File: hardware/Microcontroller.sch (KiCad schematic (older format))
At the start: 18 parts, among them J4 ICSP, J5 SERIAL_OUT, Q1 2N3904, U4 ATMEGA64M1

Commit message: Modified schematic to use one less op-amp and a cheaper microcontroller
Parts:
- removed U4: ATMEGA64M1, TQFP-32, symbol ATMEGA64M1
- added C12, C13: 18pF, 0805, symbol C
- added U3: ATMEGA328-A, TQFP32, symbol ATMEGA328-A
- added X1: 20MHz, HC49, symbol CRYSTAL
- renumbered C11 to C10, C14 to C11, C15 to C14, C12 to C8, C13 to C9, R14 to R10, R15 to R11, R16 to R12, R17 to R13, R18 to R14, R19 to R15, R13 to R9
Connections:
- net labels added: CURR_SENSE, MISO, MOSI, SCK
- net labels removed: U_CURR_SENSE, V_CURR_SENSE, W_CURR_SENSE
- wire segments 63 -> 73
- no-connect marks 10 -> 5
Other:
- moved on the sheet: C10, C11, C8, C9, R12

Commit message: Modified schemdatic to use a single PWM channel, similar to Atmel's app note.
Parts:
- added C21: 1uF, 0805, symbol C
- added D4: LED, symbol LED
- added R14: 11k, 0805, symbol R
- added R19: 1k, 0805, symbol R
- added SW1: SW_PUSH, symbol SW_PUSH
- added U4: 74LV08, symbol 74LS08
- C11, C14: value 1000pF -> 2000pF
- R10: renamed from R9; value 10.2K -> 11K
- R11: renamed from R10; value 10.2K -> 11K
- R12: renamed from R11; value 10.2K -> 11K
- R13: renamed from R12; value 10.2K -> 11k
- R16: renamed from R14; value 57.6K -> 169k
- R17: renamed from R15; value 10.2K -> 11k
- renumbered JP1 to J5, J5 to J6, R13 to R15
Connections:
- net labels added: DEBUG_LED, PWM, U_HI_EN, V_HI_EN, W_HI_EN
- net labels removed: BATT_PWM
- wire segments 73 -> 98
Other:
- moved on the sheet: C14, J4, J5, J6, Q1, R10, R11, R12, R15, R16, R17

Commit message: Changed most parts to be through hole to simplify the initial prototype assembly
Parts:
- removed C21: 1uF, 0805, symbol C
- removed L1: 1k @ 100MHz, 0805, symbol INDUCTOR
- removed U3: ATMEGA328-A, TQFP32, symbol ATMEGA328-A
- added C15: 2000pF, symbol C
- added U3: ATMEGA328-P, DIL28, symbol ATMEGA328-P
- C10, C8, C9: footprint 0805 -> (none); Digikey P/N 1276-3010-1-ND -> 445-8517-ND; Mfg P/N CL21F105ZBFNNNE -> FK24X7R1H105K; Mouser P/N (none) -> 810-FK24X7R1H105K
- C11: footprint 0805 -> (none); Digikey P/N 1276-1020-1-ND -> 1268PH-ND; Mfg P/N CL21B102KBANNNC -> S202M29Z5UN63L6R; Mouser P/N (none) -> 594-S202M29Z5UN63L6R
- C12, C13: footprint 0805 -> (none); Digikey P/N 1276-1107-1-ND -> 445-4762-ND; Mfg P/N CL21C180JBANNNC -> FK18C0G1H180J; Mouser P/N (none) -> 810-FK18C0G1H180J
- C14: value 2000pF -> 1uF; footprint 0805 -> (none); Digikey P/N 1276-1020-1-ND -> 445-8517-ND; Mfg P/N CL21B102KBANNNC -> FK24X7R1H105K; Mouser P/N (none) -> 810-FK24X7R1H105K
- R10, R11, R12: value 11K -> 11k; footprint 0805 -> (none); Digikey P/N P10.2KCCT-ND -> 11.0KXBK-ND; Mfg P/N ERJ-6ENF1022V -> MFR-25FBF52-11K; Mouser P/N 667-ERJ-6ENF1022V -> 603-MFR-25FBF52-11K
- R13, R14, R17: footprint 0805 -> (none); Digikey P/N P10.2KCCT-ND -> 11.0KXBK-ND; Mfg P/N ERJ-6ENF1022V -> MFR-25FBF52-11K; Mouser P/N 667-ERJ-6ENF1022V -> 603-MFR-25FBF52-11K
- R15: value 1K -> 1k; footprint 0805 -> (none); Digikey P/N P1.00KCCT-ND -> 1.00KXBK-ND; Mfg P/N ERJ-6ENF1001V -> MFR-25FBF52-1K; Mouser P/N 667-ERJ-6ENF1001V -> 603-MFR-25FBF52-1K
- R16: footprint 0805 -> (none); Digikey P/N P56.2KCCT-ND -> 169KXBK-ND; Mfg P/N ERJ-6ENF5622V -> MFR-25FBF52-169K; Mouser P/N 667-ERJ-6ENF5622V -> 603-MFR-25FBF52-169K
- R19: footprint 0805 -> (none); Digikey P/N P10.2KCCT-ND -> 1.00KXBK-ND; Mfg P/N ERJ-6ENF1022V -> MFR-25FBF52-1K; Mouser P/N 667-ERJ-6ENF1022V -> 603-MFR-25FBF52-1K
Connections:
- net labels removed: +5VA
- wire segments 98 -> 93
- no-connect marks 5 -> 3

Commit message: Added inital layout revision.
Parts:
- U4: value 74LV08 -> 74HC08; Digikey P/N 296-26531-1-ND -> 296-1570-5-ND; Mfg P/N SN74LV08ADR -> SN74HC08N; Mouser P/N 595-SN74LV08ADR -> 595-SN74HC08N
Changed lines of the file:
@@
-EESchema Schematic File Version 2  date Wed 20 May 2015 21:52:57 MST
+EESchema Schematic File Version 2  date Sun 14 Jun 2015 10:56:58 MST
 LIBS:power
 LIBS:device
@@
 Sheet 3 4
 Title "Microcontroller and Support"
-Date "21 may 2015"
+Date "14 jun 2015"
 Rev ""
 Comp ""
@@
 Comment4 ""
 $EndDescr
+$Comp
+L 74LS08 U4
+U 4 1 557DAFC6
+P 8350 3800
+F 0 "U4" H 8350 3850 60  0000 C CNN
+F 1 "74HC08" H 8350 3750 60  0000 C CNN
+F 3 "datasheets/sn74hc08.pdf" H 8350 3800 60  0001 C CNN
+F 4 "SN74HC08N" H 8350 3800 60  0001 C CNN "Mfg P/N"
+F 5 "296-1570-5-ND" H 8350 3800 60  0001 C CNN "Digikey P/N"
+F 6 "595-SN74HC08N" H 8350 3800 60  0001 C CNN "Mouser P/N"
+	4    8350 3800
+	1    0    0    -1
+$EndComp
+$Comp
+L 74LS08 U4
+U 3 1 557DAFC4
+P 8350 3350
+F 0 "U4" H 8350 3400 60  0000 C CNN
+F 1 "74HC08" H 8350 3300 60  0000 C CNN
+F 3 "datasheets/sn74hc08.pdf" H 8350 3350 60  0001 C CNN
+F 4 "SN74HC08N" H 8350 3350 60  0001 C CNN "Mfg P/N"
+F 5 "296-1570-5-ND" H 8350 3350 60  0001 C CNN "Digikey P/N"
+F 6 "595-SN74HC08N" H 8350 3350 60  0001 C CNN "Mouser P/N"
+	3    8350 3350
+	1    0    0    -1
+$EndComp
+$Comp
+L 74LS08 U4
+U 2 1 557DAFC2
+P 8350 2900
+F 0 "U4" H 8350 2950 60  0000 C CNN
+F 1 "74HC08" H 8350 2850 60  0000 C CNN
+F 3 "datasheets/sn74hc08.pdf" H 8350 2900 60  0001 C CNN
+F 4 "SN74HC08N" H 8350 2900 60  0001 C CNN "Mfg P/N"
+F 5 "296-1570-5-ND" H 8350 2900 60  0001 C CNN "Digikey P/N"
+F 6 "595-SN74HC08N" H 8350 2900 60  0001 C CNN "Mouser P/N"
+	2    8350 2900
+	1    0    0    -1
+$EndComp
 $Comp
 L ATMEGA328-P U3
@@
 $Comp
 L 74LS08 U4
-U 4 1 554593C7
-P 8350 3800
-F 0 "U4" H 8350 3850 60  0000 C CNN
-F 1 "74LV08" H 8350 3750 60  0000 C CNN
-F 3 "datasheets/sn74lv08a.pdf" H 8350 3800 60  0001 C CNN
-F 4 "SN74LV08ADR" H 8350 3800 60  0001 C CNN "Mfg P/N"
-F 5 "296-26531-1-ND" H 8350 3800 60  0001 C CNN "Digikey P/N"
-F 6 "595-SN74LV08ADR" H 8350 3800 60  0001 C CNN "Mouser P/N"
-	4    8350 3800
-	1    0    0    -1
-$EndComp
-$Comp
-L 74LS08 U4
-U 3 1 554593C5
-P 8350 3350
-F 0 "U4" H 8350 3400 60  0000 C CNN
-F 1 "74LV08" H 8350 3300 60  0000 C CNN
-F 3 "datasheets/sn74lv08a.pdf" H 8350 3350 60  0001 C CNN
-F 4 "SN74LV08ADR" H 8350 3350 60  0001 C CNN "Mfg P/N"
-F 5 "296-26531-1-ND" H 8350 3350 60  0001 C CNN "Digikey P/N"
-F 6 "595-SN74LV08ADR" H 8350 3350 60  0001 C CNN "Mouser P/N"
-	3    8350 3350
-	1    0    0    -1
-$EndComp
-$Comp
-L 74LS08 U4
-U 2 1 554593C3
-P 8350 2900
-F 0 "U4" H 8350 2950 60  0000 C CNN
-F 1 "74LV08" H 8350 2850 60  0000 C CNN
-F 3 "datasheets/sn74lv08a.pdf" H 8350 2900 60  0001 C CNN
-F 4 "SN74LV08ADR" H 8350 2900 60  0001 C CNN "Mfg P/N"
-F 5 "296-26531-1-ND" H 8350 2900 60  0001 C CNN "Digikey P/N"
-F 6 "595-SN74LV08ADR" H 8350 2900 60  0001 C CNN "Mouser P/N"
-	2    8350 2900
-	1    0    0    -1
-$EndComp
-$Comp
-L 74LS08 U4
 U 1 1 554592E1
 P 8350 2250
 F 0 "U4" H 8350 2300 60  0000 C CNN
-F 1 "74LV08" H 8350 2200 60  0000 C CNN
-F 3 "datasheets/sn74lv08a.pdf" H 8350 2250 60  0001 C CNN
-F 4 "SN74LV08ADR" H 8350 2250 60  0001 C CNN "Mfg P/N"
-F 5 "296-26531-1-ND" H 8350 2250 60  0001 C CNN "Digikey P/N"
-F 6 "595-SN74LV08ADR" H 8350 2250 60  0001 C CNN "Mouser P/N"
+F 1 "74HC08" H 8350 2200 60  0000 C CNN
+F 3 "datasheets/sn74hc08.pdf" H 8350 2250 60  0001 C CNN
+F 4 "SN74HC08N" H 8350 2250 60  0001 C CNN "Mfg P/N"
+F 5 "296-1570-5-ND" H 8350 2250 60  0001 C CNN "Digikey P/N"
+F 6 "595-SN74HC08N" H 8350 2250 60  0001 C CNN "Mouser P/N"
 	1    8350 2250
 	1    0    0    -1

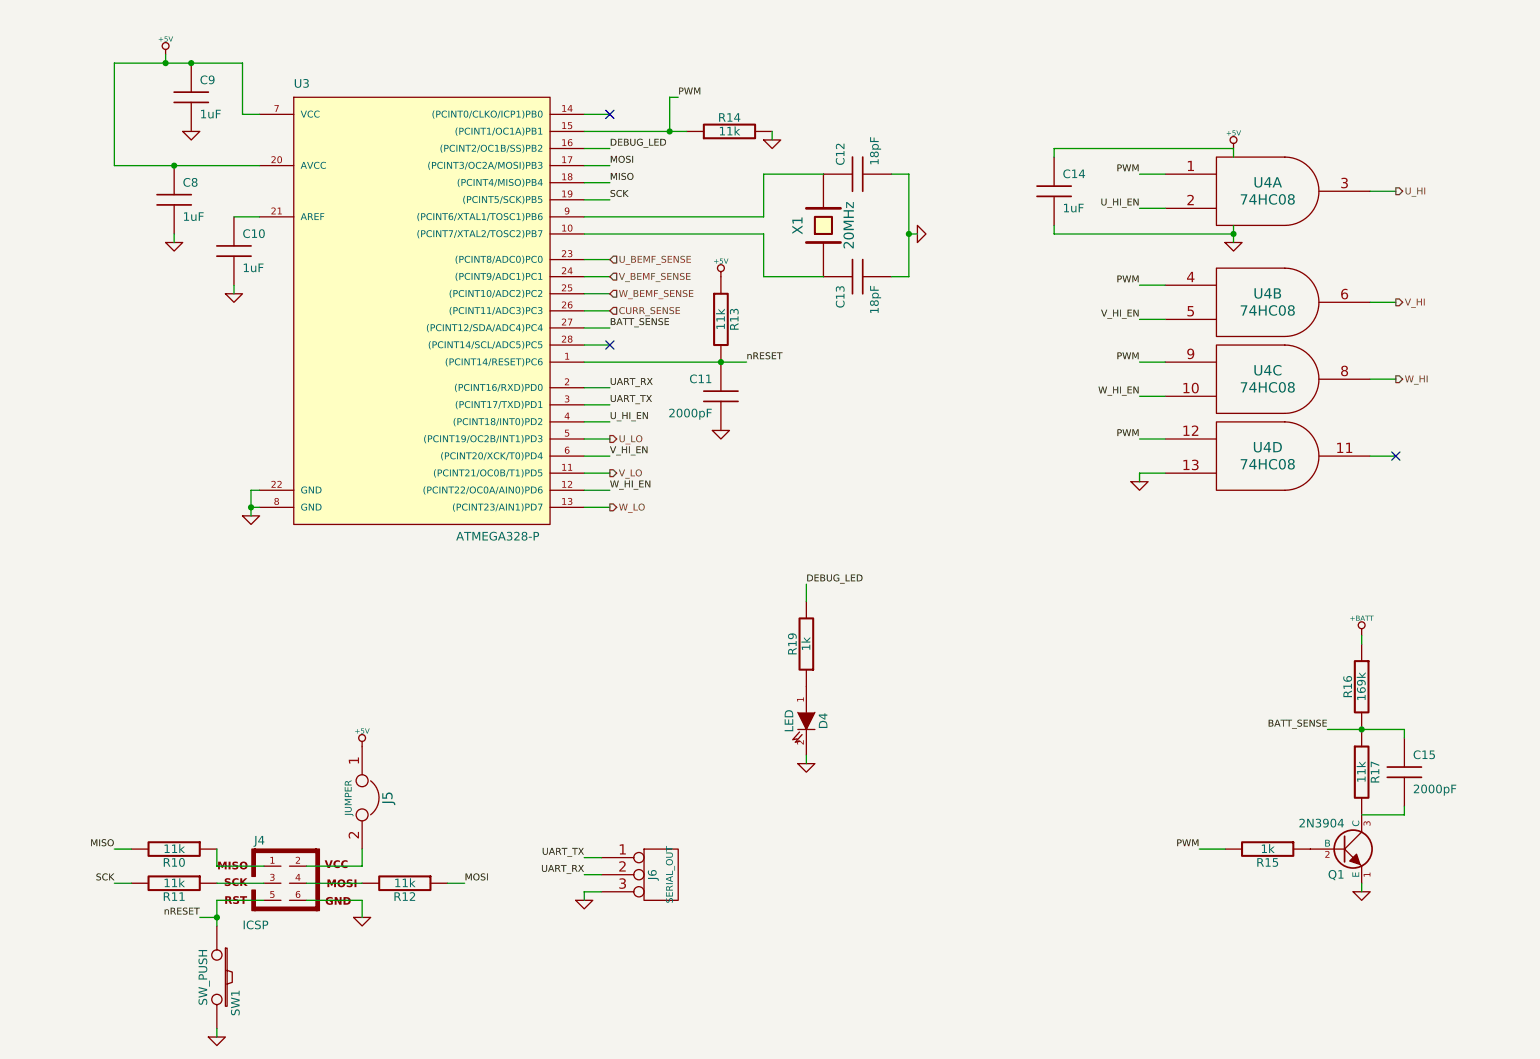
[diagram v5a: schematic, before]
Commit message: Fixed item properties and generated a BOM.
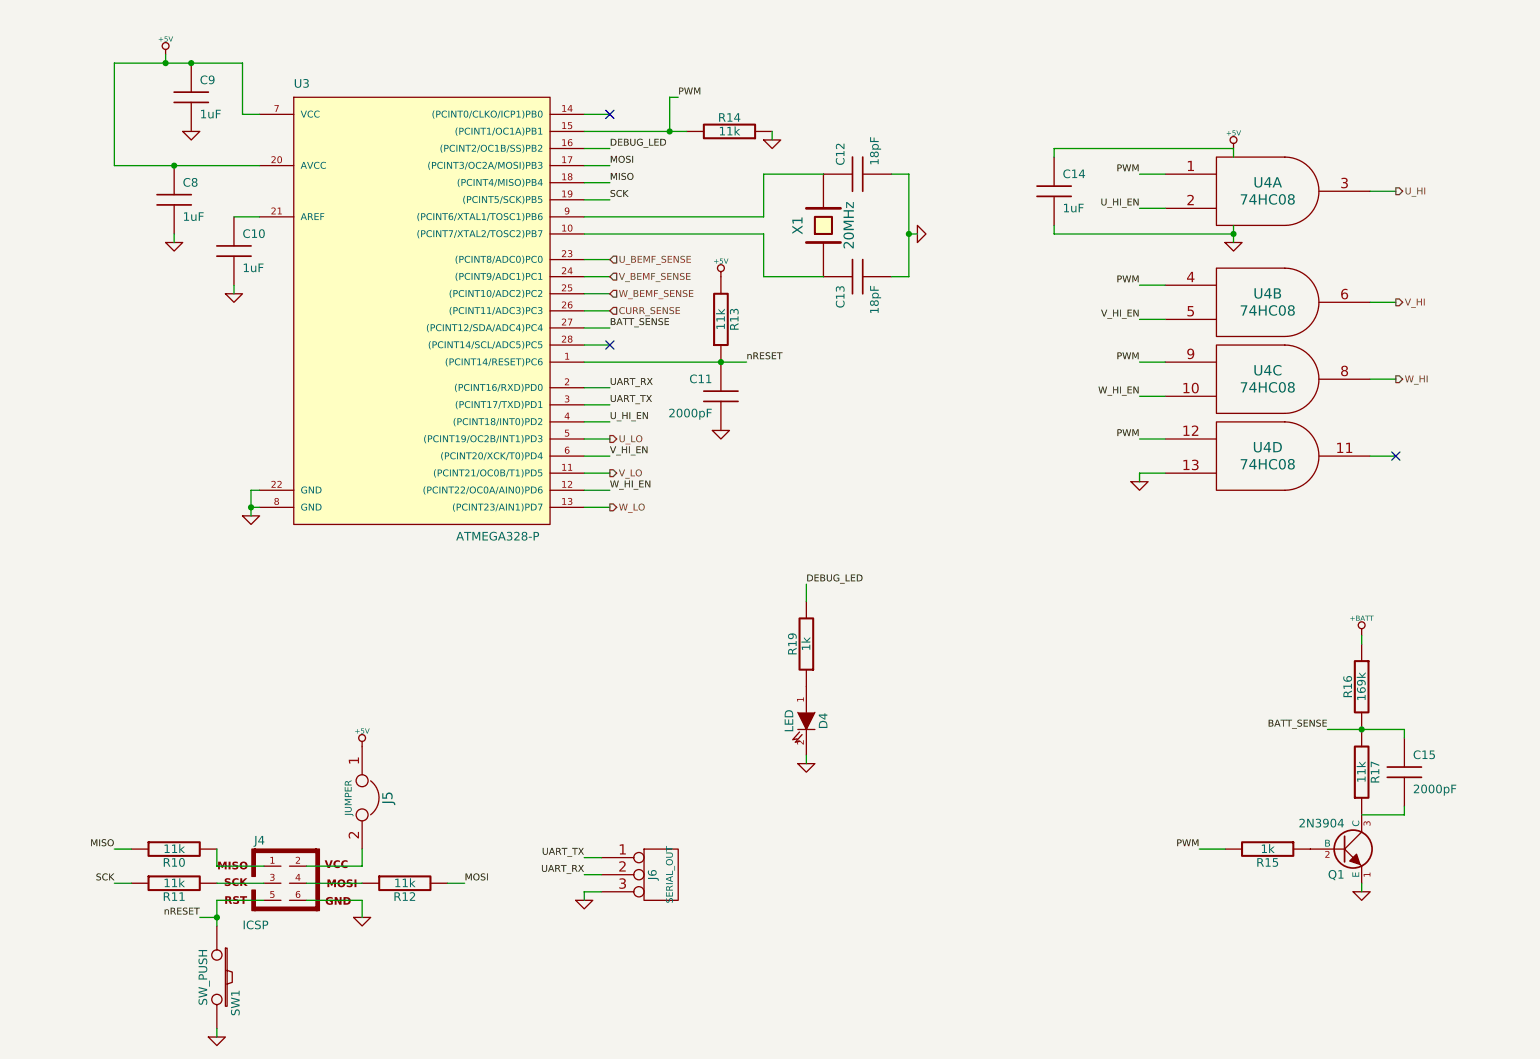
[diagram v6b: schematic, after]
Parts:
- D4: Digikey P/N (none) -> 754-1606-ND; Mfg P/N (none) -> WP710A10ID; Mouser P/N (none) -> 604-WP710A10ID
- J5: Digikey P/N (none) -> S1012EC-40-ND; Mfg P/N (none) -> PREC040SAAN-RC; Mouser P/N (none) -> N/A
- J6: Mouser P/N (none) -> N/A
- SW1: Digikey P/N (none) -> 450-1804-ND; Mfg P/N (none) -> 1825910-7; Mouser P/N (none) -> 506-FSM4JAH
- U3: Digikey P/N (none) -> ATMEGA328-PU-ND; Mfg P/N (none) -> ATMEGA328-PU; Mouser P/N (none) -> 556-ATMEGA328-PU
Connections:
- net +5V: now also R13.2; no longer R13.1
- net BATT_SENSE: now also R17.2; no longer R17.1
- net GND: now also R14.1; no longer R14.2
- net MISO: now also R10.1; no longer R10.2
- net MOSI: now also R12.2; no longer R12.1
- net PWM: now also R14.2; no longer R14.1
- net SCK: now also R11.1; no longer R11.2
- net nRESET: now also R13.1; no longer R13.2
- net at C15.2, Q1.3 (C): now also R17.1; no longer R17.2
- net at J4.1: now also R10.2; no longer R10.1
- net at J4.3: now also R11.2; no longer R11.1
- net at J4.4: now also R12.1; no longer R12.2
